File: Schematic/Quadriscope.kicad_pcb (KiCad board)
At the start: 2 copper layers, 81.3 x 110 mm, 65 parts, among them IC101 LD1117-3.3V-SOT223, J101 IN_1, J102 THRU_1, J103 IN_2, J104 THRU_2, J105 IN_3, J106 THRU_3, J107 IN_4, J108 THRU_4, J109 Conn_02x05_Odd_Even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

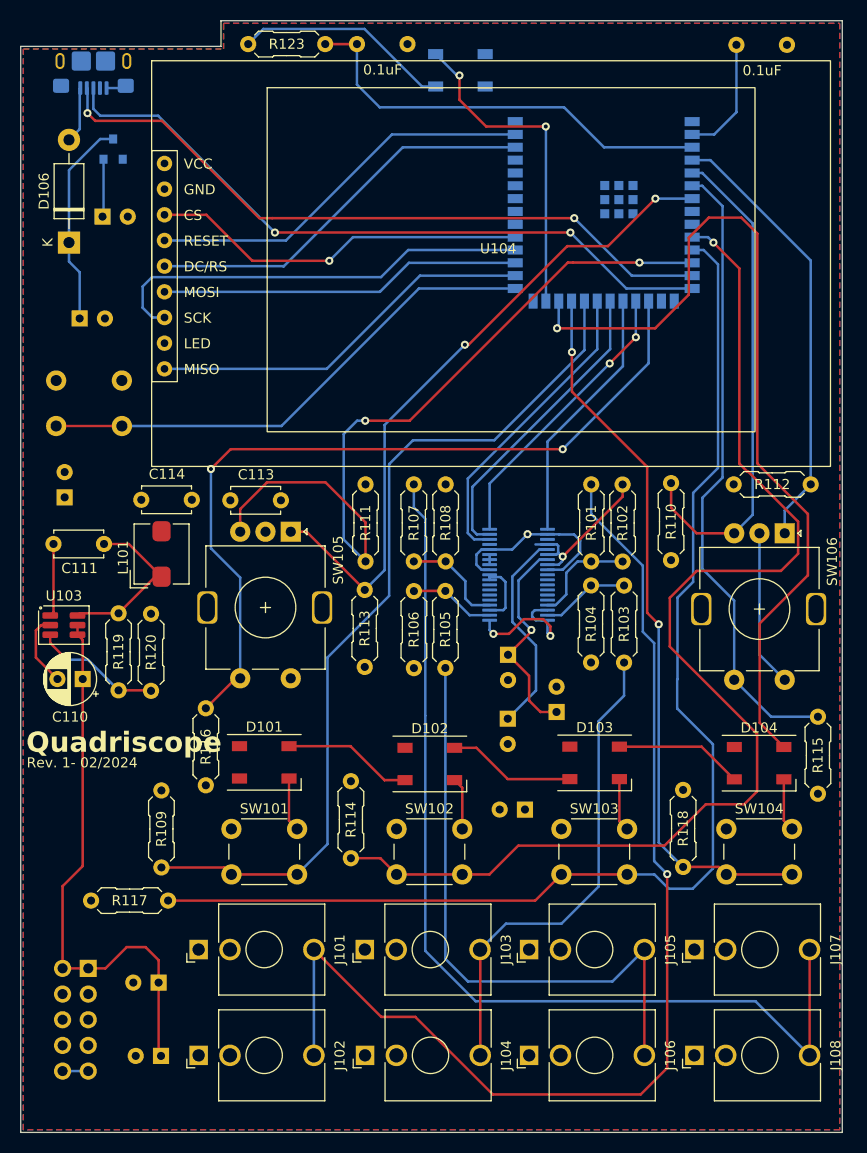
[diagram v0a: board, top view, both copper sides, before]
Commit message: new board file, interrupt stuff
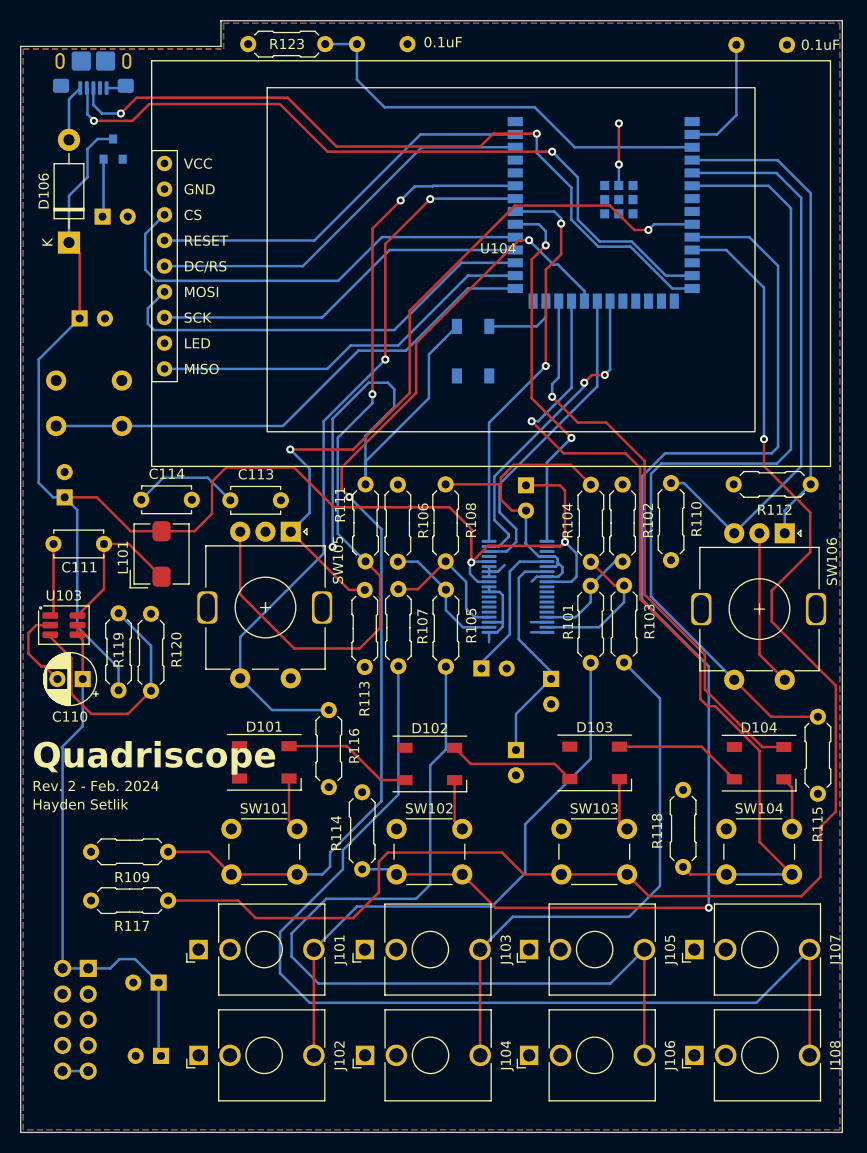
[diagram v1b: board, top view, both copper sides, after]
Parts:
- R119: value 51k -> 89k
- moved C101 32.1 mm to (50.0, -64.0), turned to -90 degrees
- moved D105 27.8 mm to (44.8, -77.3), turned to 90 degrees
- moved R107 18.0 mm to (37.4, -46.1), turned to 90 degrees
- moved R101 17.7 mm to (56.4, -46.5), turned to 90 degrees
- moved R116 12.2 mm to (30.5, -34.2)
- moved C107 9.45 mm to (49.0, -37.8)
- moved R109 9.24 mm to (6.96, -27.8), turned to 0 degrees
- moved C102 5.61 mm to (45.6, -45.9), turned to 0 degrees
- moved C106 3.32 mm to (52.5, -44.9), turned to -90 degrees
- moved R106 3.31 mm to (37.3, -56.5), turned to 90 degrees
- moved R104 2.34 mm to (56.4, -56.5), turned to 90 degrees
- moved R114 1.56 mm to (33.8, -33.7)
- moved U102 1.19 mm to (49.2, -54.0)
- moved R105 0.14 mm to (42.1, -46.1)
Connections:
- C101 pad 1: +3.3V -> +5V
- C112 pad 1: +3.3V -> +5V
- L101 pad 2: +3.3V -> +5V
- R119 pad 1: Net-(U103-SW) -> Net-(U103-FB)
- R119 pad 2: Net-(U103-FB) -> +5V
- U101 pad 12: ENCB_R -> unconnected-(U101-GPIO8/TOUCH8/ADC1_CH7/SUBSPICS1-Pad12)
- U101 pad 17: ENCB_B -> unconnected-(U101-GPIO9/TOUCH9/ADC1_CH8/FSPIHD/SUBSPIHD-Pad17)
- U101 pad 18: ADC_CS -> unconnected-(U101-GPIO10/TOUCH10/ADC1_CH9/FSPICS0/FSPIIO4/SUBSPICS0-Pad18)
- U101 pad 19: ADC_MOSI -> unconnected-(U101-GPIO11/TOUCH11/ADC2_CH0/FSPID/FSPIIO5/SUBSPID-Pad19)
- U101 pad 32: unconnected-(U101-MTCK/GPIO39/CLK_OUT3/SUBSPICS1-Pad32) -> ADC_MOSI
- U101 pad 33: unconnected-(U101-MTDO/GPIO40/CLK_OUT2-Pad33) -> ADC_CS
- U101 pad 34: unconnected-(U101-MTDI/GPIO41/CLK_OUT1-Pad34) -> ENCB_B
- U101 pad 35: unconnected-(U101-MTMS/GPIO42-Pad35) -> ENCB_R
- U101 pad 7: ENCB_L -> unconnected-(U101-GPIO7/TOUCH7/ADC1_CH6-Pad7)
- U101 pad 9: unconnected-(U101-GPIO16/U0CTS/ADC2_CH5/XTAL_32K_N-Pad9) -> ENCB_L
- U102 pad 2: +3.3V -> +5V
- U102 pad 30: +3.3V -> +5V
- U102 pad 34: +3.3V -> +5V
- U102 pad 9: +3.3V -> +5V
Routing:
- net +5V: track 20.8 -> 148.7 mm, vias 0 -> 2
- net Net-(J101-PadT): track 113.3 -> 58.0 mm, vias 1 -> 0
- net PIXELS: track 86.9 -> 56.8 mm
- net Net-(J105-PadT): track 61.2 -> 88.1 mm
- net Net-(D105-DOUT): track 32.6 -> 7.56 mm, vias 2 -> 0
- net C3: track 122.4 -> 146.0 mm, vias 0 -> 1
- net +3.3V: track 58.2 -> 79.0 mm
- net ENCA_B: track 62.6 -> 83.0 mm
- net GND: track 84.3 -> 102.6 mm, vias 3 -> 2
- net C1: track 86.9 -> 99.8 mm, vias 0 -> 2
- net C4: track 71.6 -> 84.5 mm, vias 2 -> 1
- net Net-(U103-FB): track 12.8 -> 25.4 mm, vias 1 -> 0
- net ADC_MOSI: track 25.7 -> 37.2 mm, vias 0 -> 2
- net ADC_CS: track 28.6 -> 39.7 mm
- net ENCB_L: track 66.5 -> 75.1 mm
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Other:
- board text added: "Hayden Setlik"
- board text added: "Rev. 2 - Feb. 2024"
- board text removed: "Rev. 1- 02/2024"
